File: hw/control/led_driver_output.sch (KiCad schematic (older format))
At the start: 6 parts

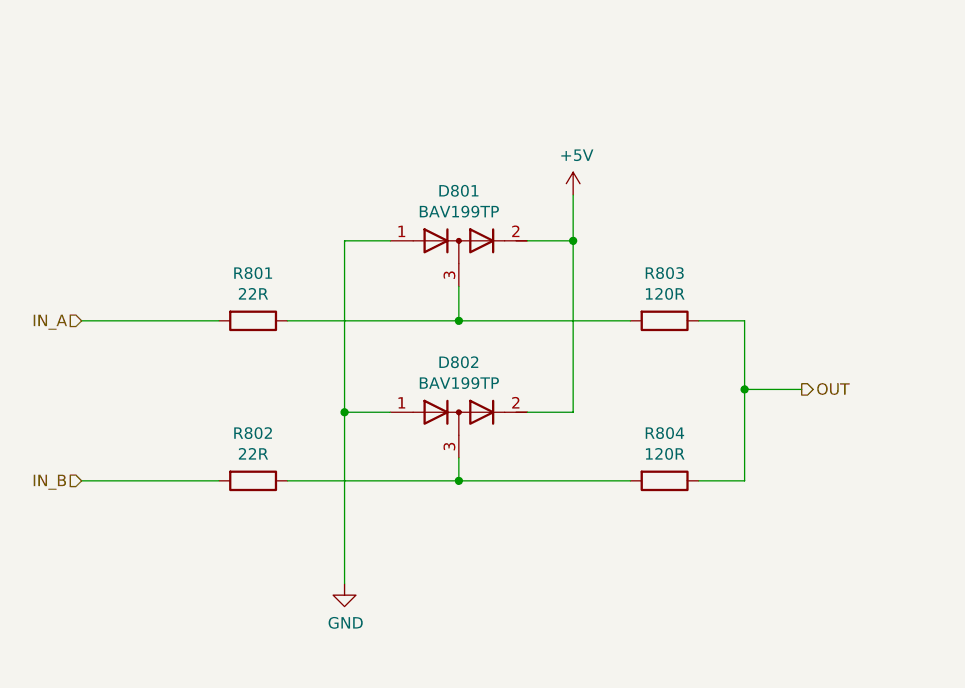
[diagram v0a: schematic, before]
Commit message: [hw] Add some component types
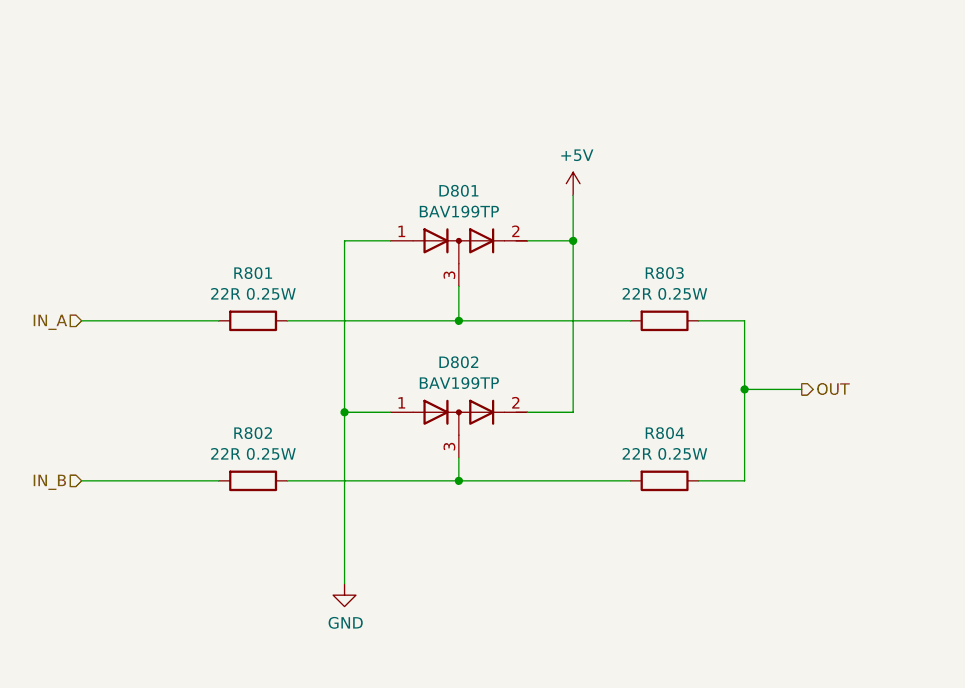
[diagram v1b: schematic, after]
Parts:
- R801, R802: value 22R -> 22R 0.25W
- R803, R804: value 120R -> 22R 0.25W
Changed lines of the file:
@@
 AR Path="/614B1933/614AD8B5/614A3B39" Ref="R901"  Part="1"
 F 0 "R801" V 4743 3750 50  0000 C CNN
-F 1 "22R" V 4834 3750 50  0000 C CNN
+F 1 "22R 0.25W" V 4834 3750 50  0000 C CNN
 F 2 "" V 4880 3750 50  0001 C CNN
 F 3 "~" H 4950 3750 50  0001 C CNN
@@
 AR Path="/614B1933/614AD8B5/614A3B3F" Ref="R903"  Part="1"
 F 0 "R803" V 6543 3750 50  0000 C CNN
-F 1 "120R" V 6634 3750 50  0000 C CNN
+F 1 "22R 0.25W" V 6634 3750 50  0000 C CNN
 F 2 "" V 6680 3750 50  0001 C CNN
 F 3 "~" H 6750 3750 50  0001 C CNN
@@
 AR Path="/614B1933/614AD8B5/614A3B45" Ref="R902"  Part="1"
 F 0 "R802" V 4743 4450 50  0000 C CNN
-F 1 "22R" V 4834 4450 50  0000 C CNN
+F 1 "22R 0.25W" V 4834 4450 50  0000 C CNN
 F 2 "" V 4880 4450 50  0001 C CNN
 F 3 "~" H 4950 4450 50  0001 C CNN
@@
 AR Path="/614B1933/614AD8B5/614A3B4B" Ref="R904"  Part="1"
 F 0 "R804" V 6543 4450 50  0000 C CNN
-F 1 "120R" V 6634 4450 50  0000 C CNN
+F 1 "22R 0.25W" V 6634 4450 50  0000 C CNN
 F 2 "" V 6680 4450 50  0001 C CNN
 F 3 "~" H 6750 4450 50  0001 C CNN

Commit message: [hw] Add some more peripherals
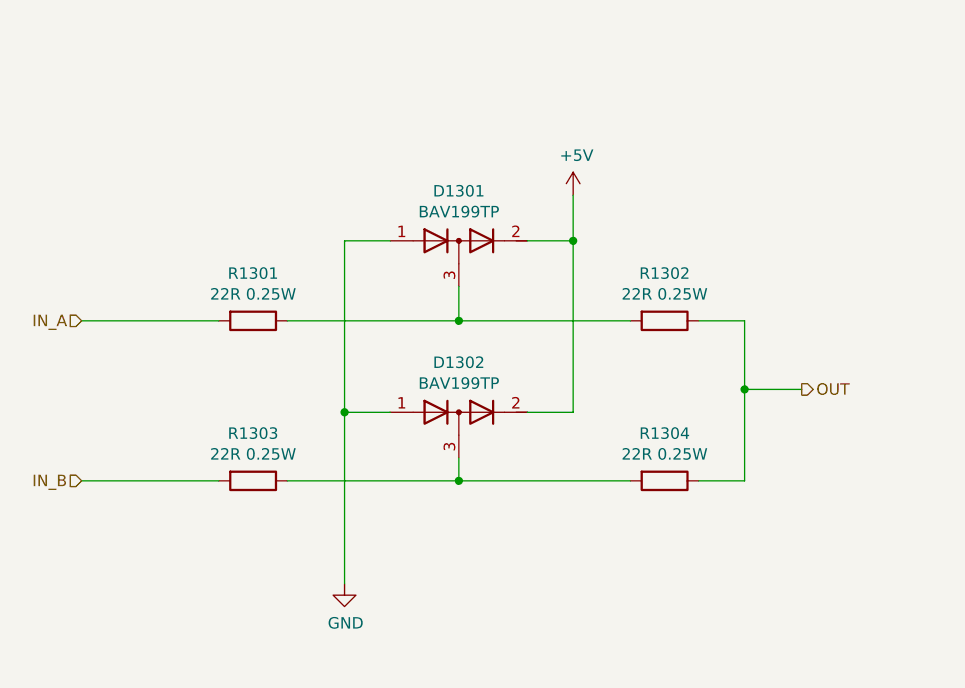
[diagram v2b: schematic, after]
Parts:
- renumbered D801 to D1201, D802 to D1202, R801 to R1201, R803 to R1202, R802 to R1203, R804 to R1204
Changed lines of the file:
@@
 $Descr A4 11693 8268
 encoding utf-8
-Sheet 8 9
+Sheet 8 13
 Title "WS2812 Controller"
-Date "2021-09-21"
+Date "2021-10-10"
 Rev "1"
 Comp "Stefan Misik"
@@
 P 4950 3750
 AR Path="/614B1933/614A3B39" Ref="R?"  Part="1"
-AR Path="/614B1933/614A1815/614A3B39" Ref="R801"  Part="1"
-AR Path="/614B1933/614AD8B5/614A3B39" Ref="R901"  Part="1"
-F 0 "R801" V 4743 3750 50  0000 C CNN
+AR Path="/614B1933/614A1815/614A3B39" Ref="R1201"  Part="1"
+AR Path="/614B1933/614AD8B5/614A3B39" Ref="R1301"  Part="1"
+F 0 "R1301" V 4743 3750 50  0000 C CNN
 F 1 "22R 0.25W" V 4834 3750 50  0000 C CNN
 F 2 "" V 4880 3750 50  0001 C CNN
@@
 P 6750 3750
 AR Path="/614B1933/614A3B3F" Ref="R?"  Part="1"
-AR Path="/614B1933/614A1815/614A3B3F" Ref="R803"  Part="1"
-AR Path="/614B1933/614AD8B5/614A3B3F" Ref="R903"  Part="1"
-F 0 "R803" V 6543 3750 50  0000 C CNN
+AR Path="/614B1933/614A1815/614A3B3F" Ref="R1202"  Part="1"
+AR Path="/614B1933/614AD8B5/614A3B3F" Ref="R1302"  Part="1"
+F 0 "R1302" V 6543 3750 50  0000 C CNN
 F 1 "22R 0.25W" V 6634 3750 50  0000 C CNN
 F 2 "" V 6680 3750 50  0001 C CNN
@@
 P 4950 4450
 AR Path="/614B1933/614A3B45" Ref="R?"  Part="1"
-AR Path="/614B1933/614A1815/614A3B45" Ref="R802"  Part="1"
-AR Path="/614B1933/614AD8B5/614A3B45" Ref="R902"  Part="1"
-F 0 "R802" V 4743 4450 50  0000 C CNN
+AR Path="/614B1933/614A1815/614A3B45" Ref="R1203"  Part="1"
+AR Path="/614B1933/614AD8B5/614A3B45" Ref="R1303"  Part="1"
+F 0 "R1303" V 4743 4450 50  0000 C CNN
 F 1 "22R 0.25W" V 4834 4450 50  0000 C CNN
 F 2 "" V 4880 4450 50  0001 C CNN
@@
 P 6750 4450
 AR Path="/614B1933/614A3B4B" Ref="R?"  Part="1"
-AR Path="/614B1933/614A1815/614A3B4B" Ref="R804"  Part="1"
-AR Path="/614B1933/614AD8B5/614A3B4B" Ref="R904"  Part="1"
-F 0 "R804" V 6543 4450 50  0000 C CNN
+AR Path="/614B1933/614A1815/614A3B4B" Ref="R1204"  Part="1"
+AR Path="/614B1933/614AD8B5/614A3B4B" Ref="R1304"  Part="1"
+F 0 "R1304" V 6543 4450 50  0000 C CNN
 F 1 "22R 0.25W" V 6634 4450 50  0000 C CNN
 F 2 "" V 6680 4450 50  0001 C CNN
@@
 P 5850 3400
 AR Path="/614B1933/614A3B51" Ref="D?"  Part="1"
-AR Path="/614B1933/614A1815/614A3B51" Ref="D801"  Part="1"
-AR Path="/614B1933/614AD8B5/614A3B51" Ref="D901"  Part="1"
-F 0 "D801" H 5850 3617 50  0000 C CNN
+AR Path="/614B1933/614A1815/614A3B51" Ref="D1201"  Part="1"
+AR Path="/614B1933/614AD8B5/614A3B51" Ref="D1301"  Part="1"
+F 0 "D1301" H 5850 3617 50  0000 C CNN
 F 1 "BAV199TP" H 5850 3526 50  0000 C CNN
 F 2 "Package_TO_SOT_SMD:SOT-23" H 5850 2900 50  0001 C CNN
@@
 P 5850 4150
 AR Path="/614B1933/614A3B57" Ref="D?"  Part="1"
-AR Path="/614B1933/614A1815/614A3B57" Ref="D802"  Part="1"
-AR Path="/614B1933/614AD8B5/614A3B57" Ref="D902"  Part="1"
-F 0 "D802" H 5850 4367 50  0000 C CNN
+AR Path="/614B1933/614A1815/614A3B57" Ref="D1202"  Part="1"
+AR Path="/614B1933/614AD8B5/614A3B57" Ref="D1302"  Part="1"
+F 0 "D1302" H 5850 4367 50  0000 C CNN
 F 1 "BAV199TP" H 5850 4276 50  0000 C CNN
 F 2 "Package_TO_SOT_SMD:SOT-23" H 5850 3650 50  0001 C CNN
@@
 P 6350 3200
 AR Path="/614B1933/614A3B70" Ref="#PWR?"  Part="1"
-AR Path="/614B1933/614A1815/614A3B70" Ref="#PWR0802"  Part="1"
-AR Path="/614B1933/614AD8B5/614A3B70" Ref="#PWR0902"  Part="1"
-F 0 "#PWR0802" H 6350 3050 50  0001 C CNN
+AR Path="/614B1933/614A1815/614A3B70" Ref="#PWR01201"  Part="1"
+AR Path="/614B1933/614AD8B5/614A3B70" Ref="#PWR01301"  Part="1"
+F 0 "#PWR01301" H 6350 3050 50  0001 C CNN
 F 1 "+5V" H 6365 3373 50  0000 C CNN
 F 2 "" H 6350 3200 50  0001 C CNN
@@
 Connection ~ 5350 4150
 $Comp
-L power:GND #PWR0801
+L power:GND #PWR01202
 U 1 1 614A4F14
 P 5350 4900
-AR Path="/614B1933/614A1815/614A4F14" Ref="#PWR0801"  Part="1"
-AR Path="/614B1933/614AD8B5/614A4F14" Ref="#PWR0901"  Part="1"
-F 0 "#PWR0801" H 5350 4650 50  0001 C CNN
+AR Path="/614B1933/614A1815/614A4F14" Ref="#PWR01202"  Part="1"
+AR Path="/614B1933/614AD8B5/614A4F14" Ref="#PWR01302"  Part="1"
+F 0 "#PWR01302" H 5350 4650 50  0001 C CNN
 F 1 "GND" H 5355 4727 50  0000 C CNN
 F 2 "" H 5350 4900 50  0001 C CNN

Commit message: [hw] Add alternative LED data line from SPI
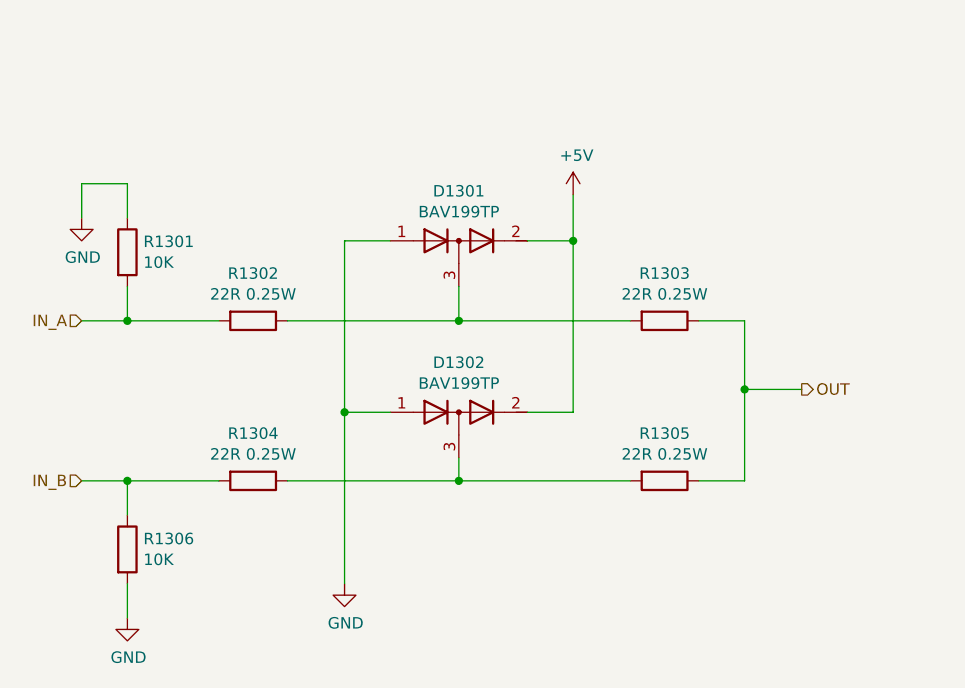
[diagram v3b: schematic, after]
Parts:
- added R1201, R1206: 10K, symbol Device:R
- renumbered R1201 to R1202, R1202 to R1203, R1203 to R1204, R1204 to R1205
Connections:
- net GND: now also R1201.1, R1206.2
- net IN_A: now also R1201.2
- net IN_B: now also R1206.1
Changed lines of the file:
@@
 $Descr A4 11693 8268
 encoding utf-8
-Sheet 8 13
+Sheet 12 13
 Title "WS2812 Controller"
 Date "2021-10-10"
@@
 P 4950 3750
 AR Path="/614B1933/614A3B39" Ref="R?"  Part="1"
-AR Path="/614B1933/614A1815/614A3B39" Ref="R1201"  Part="1"
-AR Path="/614B1933/614AD8B5/614A3B39" Ref="R1301"  Part="1"
-F 0 "R1301" V 4743 3750 50  0000 C CNN
+AR Path="/614B1933/614A1815/614A3B39" Ref="R1202"  Part="1"
+AR Path="/614B1933/614AD8B5/614A3B39" Ref="R1302"  Part="1"
+F 0 "R1302" V 4743 3750 50  0000 C CNN
 F 1 "22R 0.25W" V 4834 3750 50  0000 C CNN
 F 2 "" V 4880 3750 50  0001 C CNN
@@
 P 6750 3750
 AR Path="/614B1933/614A3B3F" Ref="R?"  Part="1"
-AR Path="/614B1933/614A1815/614A3B3F" Ref="R1202"  Part="1"
-AR Path="/614B1933/614AD8B5/614A3B3F" Ref="R1302"  Part="1"
-F 0 "R1302" V 6543 3750 50  0000 C CNN
+AR Path="/614B1933/614A1815/614A3B3F" Ref="R1203"  Part="1"
+AR Path="/614B1933/614AD8B5/614A3B3F" Ref="R1303"  Part="1"
+F 0 "R1303" V 6543 3750 50  0000 C CNN
 F 1 "22R 0.25W" V 6634 3750 50  0000 C CNN
 F 2 "" V 6680 3750 50  0001 C CNN
@@
 P 4950 4450
 AR Path="/614B1933/614A3B45" Ref="R?"  Part="1"
-AR Path="/614B1933/614A1815/614A3B45" Ref="R1203"  Part="1"
-AR Path="/614B1933/614AD8B5/614A3B45" Ref="R1303"  Part="1"
-F 0 "R1303" V 4743 4450 50  0000 C CNN
+AR Path="/614B1933/614A1815/614A3B45" Ref="R1204"  Part="1"
+AR Path="/614B1933/614AD8B5/614A3B45" Ref="R1304"  Part="1"
+F 0 "R1304" V 4743 4450 50  0000 C CNN
 F 1 "22R 0.25W" V 4834 4450 50  0000 C CNN
 F 2 "" V 4880 4450 50  0001 C CNN
@@
 P 6750 4450
 AR Path="/614B1933/614A3B4B" Ref="R?"  Part="1"
-AR Path="/614B1933/614A1815/614A3B4B" Ref="R1204"  Part="1"
-AR Path="/614B1933/614AD8B5/614A3B4B" Ref="R1304"  Part="1"
-F 0 "R1304" V 6543 4450 50  0000 C CNN
+AR Path="/614B1933/614A1815/614A3B4B" Ref="R1205"  Part="1"
+AR Path="/614B1933/614AD8B5/614A3B4B" Ref="R1305"  Part="1"
+F 0 "R1305" V 6543 4450 50  0000 C CNN
 F 1 "22R 0.25W" V 6634 4450 50  0000 C CNN
 F 2 "" V 6680 4450 50  0001 C CNN
@@
 	7100 4050 7100 3750
 Wire Wire Line
-	4200 4450 4800 4450
+	4200 4450 4400 4450
 $Comp
 L power:+5V #PWR?
@@
 Connection ~ 5350 4150
 $Comp
-L power:GND #PWR01202
+L power:GND #PWR01203
 U 1 1 614A4F14
 P 5350 4900
-AR Path="/614B1933/614A1815/614A4F14" Ref="#PWR01202"  Part="1"
-AR Path="/614B1933/614AD8B5/614A4F14" Ref="#PWR01302"  Part="1"
-F 0 "#PWR01302" H 5350 4650 50  0001 C CNN
+AR Path="/614B1933/614A1815/614A4F14" Ref="#PWR01203"  Part="1"
+AR Path="/614B1933/614AD8B5/614A4F14" Ref="#PWR01303"  Part="1"
+F 0 "#PWR01303" H 5350 4650 50  0001 C CNN
 F 1 "GND" H 5355 4727 50  0000 C CNN
 F 2 "" H 5350 4900 50  0001 C CNN
@@
 OUT
 Wire Wire Line
-	4200 3750 4800 3750
+	4200 3750 4400 3750
+$Comp
+L Device:R R1201
+U 1 1 616363D2
+P 4400 3450
+AR Path="/614B1933/614A1815/616363D2" Ref="R1201"  Part="1"
+AR Path="/614B1933/614AD8B5/616363D2" Ref="R1301"  Part="1"
+F 0 "R1301" H 4470 3496 50  0000 L CNN
+F 1 "10K" H 4470 3405 50  0000 L CNN
+F 2 "" V 4330 3450 50  0001 C CNN
+F 3 "~" H 4400 3450 50  0001 C CNN
+	1    4400 3450
+	1    0    0    -1
+$EndComp
+$Comp
+L Device:R R1206
+U 1 1 61637113
+P 4400 4750
+AR Path="/614B1933/614A1815/61637113" Ref="R1206"  Part="1"
+AR Path="/614B1933/614AD8B5/61637113" Ref="R1306"  Part="1"
+F 0 "R1306" H 4470 4796 50  0000 L CNN
+F 1 "10K" H 4470 4705 50  0000 L CNN
+F 2 "" V 4330 4750 50  0001 C CNN
+F 3 "~" H 4400 4750 50  0001 C CNN
+	1    4400 4750
+	1    0    0    -1
+$EndComp
+$Comp
+L power:GND #PWR01202
+U 1 1 61637D81
+P 4200 3300
+AR Path="/614B1933/614A1815/61637D81" Ref="#PWR01202"  Part="1"
+AR Path="/614B1933/614AD8B5/61637D81" Ref="#PWR01302"  Part="1"
+F 0 "#PWR01302" H 4200 3050 50  0001 C CNN
+F 1 "GND" H 4205 3127 50  0000 C CNN
+F 2 "" H 4200 3300 50  0001 C CNN
+F 3 "" H 4200 3300 50  0001 C CNN
+	1    4200 3300
+	1    0    0    -1
+$EndComp
+$Comp
+L power:GND #PWR01204
+U 1 1 6163895E
+P 4400 5050
+AR Path="/614B1933/614A1815/6163895E" Ref="#PWR01204"  Part="1"
+AR Path="/614B1933/614AD8B5/6163895E" Ref="#PWR01304"  Part="1"
+F 0 "#PWR01304" H 4400 4800 50  0001 C CNN
+F 1 "GND" H 4405 4877 50  0000 C CNN
+F 2 "" H 4400 5050 50  0001 C CNN
+F 3 "" H 4400 5050 50  0001 C CNN
+	1    4400 5050
+	1    0    0    -1
+$EndComp
+Wire Wire Line
+	4400 4900 4400 5050
+Wire Wire Line
+	4400 4600 4400 4450
+Connection ~ 4400 4450
+Wire Wire Line
+	4400 4450 4800 4450
+Wire Wire Line
+	4400 3600 4400 3750
+Connection ~ 4400 3750
+Wire Wire Line
+	4400 3750 4800 3750
+Wire Wire Line
+	4400 3300 4400 3150
+Wire Wire Line
+	4400 3150 4200 3150
+Wire Wire Line
+	4200 3150 4200 3300
 $EndSCHEMATC

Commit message: [hw] Assign most of the controller footprints
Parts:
- R1201, R1206: footprint (none) -> Resistor_SMD:R_0805_2012Metric_Pad1.20x1.40mm_HandSolder
- R1202, R1203, R1204, R1205: footprint (none) -> Resistor_SMD:R_1206_3216Metric_Pad1.30x1.75mm_HandSolder
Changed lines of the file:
@@
 $Descr A4 11693 8268
 encoding utf-8
-Sheet 12 13
+Sheet 13 13
 Title "WS2812 Controller"
 Date "2021-10-10"
@@
 F 0 "R1302" V 4743 3750 50  0000 C CNN
 F 1 "22R 0.25W" V 4834 3750 50  0000 C CNN
-F 2 "" V 4880 3750 50  0001 C CNN
+F 2 "Resistor_SMD:R_1206_3216Metric_Pad1.30x1.75mm_HandSolder" V 4880 3750 50  0001 C CNN
 F 3 "~" H 4950 3750 50  0001 C CNN
 	1    4950 3750
@@
 F 0 "R1303" V 6543 3750 50  0000 C CNN
 F 1 "22R 0.25W" V 6634 3750 50  0000 C CNN
-F 2 "" V 6680 3750 50  0001 C CNN
+F 2 "Resistor_SMD:R_1206_3216Metric_Pad1.30x1.75mm_HandSolder" V 6680 3750 50  0001 C CNN
 F 3 "~" H 6750 3750 50  0001 C CNN
 	1    6750 3750
@@
 F 0 "R1304" V 4743 4450 50  0000 C CNN
 F 1 "22R 0.25W" V 4834 4450 50  0000 C CNN
-F 2 "" V 4880 4450 50  0001 C CNN
+F 2 "Resistor_SMD:R_1206_3216Metric_Pad1.30x1.75mm_HandSolder" V 4880 4450 50  0001 C CNN
 F 3 "~" H 4950 4450 50  0001 C CNN
 	1    4950 4450
@@
 F 0 "R1305" V 6543 4450 50  0000 C CNN
 F 1 "22R 0.25W" V 6634 4450 50  0000 C CNN
-F 2 "" V 6680 4450 50  0001 C CNN
+F 2 "Resistor_SMD:R_1206_3216Metric_Pad1.30x1.75mm_HandSolder" V 6680 4450 50  0001 C CNN
 F 3 "~" H 6750 4450 50  0001 C CNN
 	1    6750 4450
@@
 F 0 "R1301" H 4470 3496 50  0000 L CNN
 F 1 "10K" H 4470 3405 50  0000 L CNN
-F 2 "" V 4330 3450 50  0001 C CNN
+F 2 "Resistor_SMD:R_0805_2012Metric_Pad1.20x1.40mm_HandSolder" V 4330 3450 50  0001 C CNN
 F 3 "~" H 4400 3450 50  0001 C CNN
 	1    4400 3450
@@
 F 0 "R1306" H 4470 4796 50  0000 L CNN
 F 1 "10K" H 4470 4705 50  0000 L CNN
-F 2 "" V 4330 4750 50  0001 C CNN
+F 2 "Resistor_SMD:R_0805_2012Metric_Pad1.20x1.40mm_HandSolder" V 4330 4750 50  0001 C CNN
 F 3 "~" H 4400 4750 50  0001 C CNN
 	1    4400 4750
